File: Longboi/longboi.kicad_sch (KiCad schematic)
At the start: 190 parts, among them J2 ICSP_Header, K0 KEYSW, K1 KEYSW, K10 KEYSW, K11 KEYSW, K12 KEYSW, K13 KEYSW, K14 KEYSW, K15 KEYSW, K16 KEYSW, K17 KEYSW, K18 KEYSW, K19 KEYSW, K2 KEYSW, K20 KEYSW, K21 KEYSW, K22 KEYSW, K22-spacer1 KEYSW, K22-stepped1 KEYSW, K23 KEYSW, K24 KEYSW, K25 KEYSW, K26 KEYSW, K27 KEYSW, K28 KEYSW, K29 KEYSW, K3 KEYSW, K3-2uVert1 KEYSW, K30 KEYSW, K31 KEYSW, K32 KEYSW, K33 KEYSW, K34 KEYSW, K35 KEYSW, K36 KEYSW, K37 KEYSW, K38 KEYSW, K38-2uVert1 KEYSW, K39 KEYSW, K39-spacer1 KEYSW, K4 KEYSW, K4-spacer1 KEYSW, K40 KEYSW, K41 KEYSW, K42 KEYSW, K43 KEYSW, K44 KEYSW, K45 KEYSW, K46 KEYSW, K47 KEYSW, K48 KEYSW, K49 KEYSW, K5 KEYSW, K50 KEYSW, K51 KEYSW, K52 KEYSW, K52-1u1 KEYSW, K52-2u1 KEYSW, K53 KEYSW, K54 KEYSW, K55 KEYSW, K55-1.25 KEYSW, K55-spacer1 KEYSW, K56 KEYSW, K56-1.25 KEYSW, K57 KEYSW, K57-1.25 KEYSW, K57-1.5u1 KEYSW, K57-1u1 KEYSW, K58 KEYSW, K58-6u1 KEYSW, K58for1.25Row1 KEYSW, K59 KEYSW, K59-1.25u1 KEYSW, K59-7u1 KEYSW, K59Alt1 KEYSW, K6 KEYSW, K60 KEYSW, K60Alt1 KEYSW, K61 KEYSW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

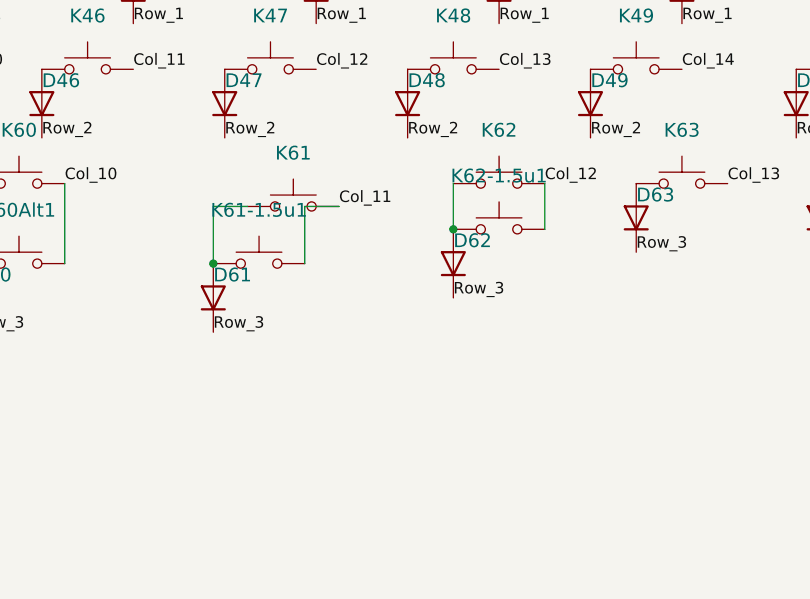
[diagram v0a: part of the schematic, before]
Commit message: update longboi to be slightly newer than ordered
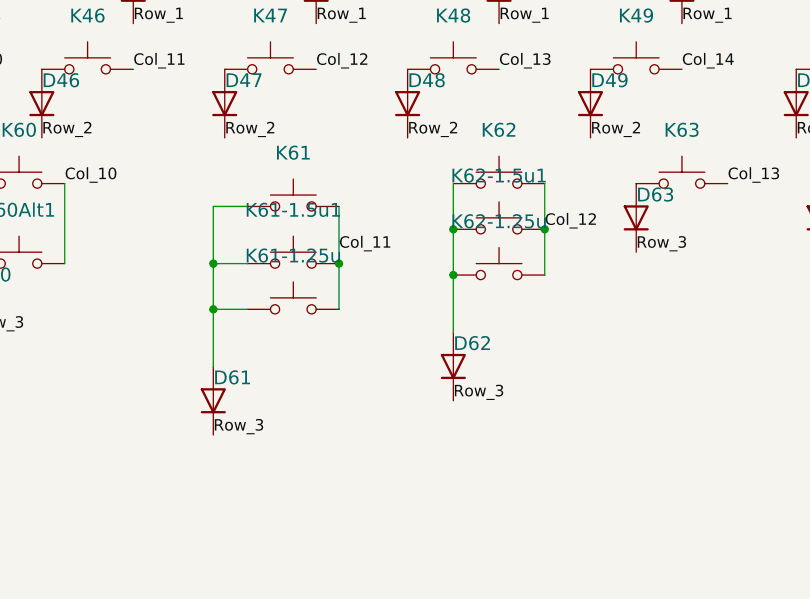
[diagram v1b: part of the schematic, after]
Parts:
- added K61-1.25u, K62-1.25u: KEYSW, MX_Only:MXOnly-1.25U-NoLED, symbol Switch:SW_Push
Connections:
- net Col_11: now also K61-1.25u.2
- net Col_12: now also K62-1.25u.2
- net at D62.2 (A), K62-1.5u1.1, K62.1: now also K62-1.25u.1
- net at D61.2 (A), K61-1.5u1.1, K61.1: now also K61-1.25u.1
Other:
- moved on the sheet: D61, D62, K61-1.5u1
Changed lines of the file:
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@@
   (junction (at 30.48 87.63) (diameter 0) (color 0 0 0 0)
   )
+  (junction (at 292.1 91.44) (diameter 0) (color 0 0 0 0)
+  )
   (junction (at 105.41 261.62) (diameter 0) (color 0 0 0 0)
   )
@@
   (junction (at 148.59 252.73) (diameter 0) (color 0 0 0 0)
   )
+  (junction (at 278.13 96.52) (diameter 0) (color 0 0 0 0)
+  )
   (junction (at 101.6 113.03) (diameter 0) (color 0 0 0 0)
   )
@@
   (junction (at 278.13 91.44) (diameter 0) (color 0 0 0 0)
   )
+  (junction (at 304.8 92.71) (diameter 0) (color 0 0 0 0)
+  )
   (junction (at 149.86 88.9) (diameter 0) (color 0 0 0 0)
   )
@@
   (junction (at 218.44 105.41) (diameter 0) (color 0 0 0 0)
   )
+  (junction (at 314.96 87.63) (diameter 0) (color 0 0 0 0)
+  )
   (junction (at 228.6 91.44) (diameter 0) (color 0 0 0 0)
   )
@@
     (stroke (width 0) (type default) (color 0 0 0 0))
   )
+  (wire (pts (xy 278.13 102.87) (xy 278.13 96.52))
+    (stroke (width 0) (type default) (color 0 0 0 0))
+  )
   (wire (pts (xy 228.6 91.44) (xy 228.6 82.55))
     (stroke (width 0) (type default) (color 0 0 0 0))
@@
     (stroke (width 0) (type default) (color 0 0 0 0))
   )
+  (wire (pts (xy 304.8 92.71) (xy 304.8 87.63))
+    (stroke (width 0) (type default) (color 0 0 0 0))
+  )
   (wire (pts (xy 403.86 35.56) (xy 405.13 35.56))
     (stroke (width 0) (type default) (color 0 0 0 0))
@@
     (stroke (width 0) (type default) (color 0 0 0 0))
   )
-  (wire (pts (xy 288.29 91.44) (xy 288.29 85.09))
-    (stroke (width 0) (type default) (color 0 0 0 0))
-  )
   (wire (pts (xy 152.4 229.87) (xy 152.4 218.44))
     (stroke (width 0) (type default) (color 0 0 0 0))
@@
     (stroke (width 0) (type default) (color 0 0 0 0))
   )
-  (wire (pts (xy 314.96 87.63) (xy 314.96 82.55))
+  (wire (pts (xy 314.96 92.71) (xy 314.96 87.63))
     (stroke (width 0) (type default) (color 0 0 0 0))
   )
@@
     (stroke (width 0) (type default) (color 0 0 0 0))
   )
+  (wire (pts (xy 304.8 99.06) (xy 304.8 92.71))
+    (stroke (width 0) (type default) (color 0 0 0 0))
+  )
   (wire (pts (xy 228.6 91.44) (xy 228.6 97.79))
     (stroke (width 0) (type default) (color 0 0 0 0))
@@
     (stroke (width 0) (type default) (color 0 0 0 0))
   )
+  (wire (pts (xy 292.1 85.09) (xy 292.1 91.44))
+    (stroke (width 0) (type default) (color 0 0 0 0))
+  )
   (wire (pts (xy 128.27 237.49) (xy 128.27 247.65))
     (stroke (width 0) (type default) (color 0 0 0 0))
@@
     (stroke (width 0) (type default) (color 0 0 0 0))
   )
+  (wire (pts (xy 292.1 96.52) (xy 292.1 91.44))
+    (stroke (width 0) (type default) (color 0 0 0 0))
+  )
   (wire (pts (xy 124.46 110.49) (xy 124.46 102.87))
     (stroke (width 0) (type default) (color 0 0 0 0))
@@
     (stroke (width 0) (type default) (color 0 0 0 0))
   )
+  (wire (pts (xy 281.94 96.52) (xy 278.13 96.52))
+    (stroke (width 0) (type default) (color 0 0 0 0))
+  )
   (wire (pts (xy 156.21 252.73) (xy 153.67 252.73))
     (stroke (width 0) (type default) (color 0 0 0 0))
   )
+  (wire (pts (xy 281.94 91.44) (xy 278.13 91.44))
+    (stroke (width 0) (type default) (color 0 0 0 0))
+  )
   (wire (pts (xy 134.62 218.44) (xy 134.62 242.57))
     (stroke (width 0) (type default) (color 0 0 0 0))
@@
     (stroke (width 0) (type default) (color 0 0 0 0))
   )
-  (wire (pts (xy 288.29 85.09) (xy 292.1 85.09))
-    (stroke (width 0) (type default) (color 0 0 0 0))
-  )
   (wire (pts (xy 91.44 48.26) (xy 91.44 44.45))
     (stroke (width 0) (type default) (color 0 0 0 0))
@@
     (stroke (width 0) (type default) (color 0 0 0 0))
   )
+  (wire (pts (xy 278.13 96.52) (xy 278.13 91.44))
+    (stroke (width 0) (type default) (color 0 0 0 0))
+  )
+  (wire (pts (xy 314.96 87.63) (xy 314.96 82.55))
+    (stroke (width 0) (type default) (color 0 0 0 0))
+  )
   (wire (pts (xy 123.19 247.65) (xy 123.19 257.81))
     (stroke (width 0) (type default) (color 0 0 0 0))
@@
     (effects (font (size 1.27 1.27)) (justify left bottom))
   )
-  (label "Row_3" (at 304.8 95.25 0)
+  (label "Row_3" (at 304.8 106.68 0)
     (effects (font (size 1.27 1.27)) (justify left bottom))
   )
@@
     (effects (font (size 1.27 1.27)) (justify left bottom))
   )
-  (label "Col_12" (at 314.96 82.55 0)
+  (label "Col_12" (at 314.96 87.63 0)
     (effects (font (size 1.27 1.27)) (justify left bottom))
   )
@@
     (effects (font (size 1.27 1.27)) (justify left bottom))
   )
-  (label "Col_11" (at 292.1 85.09 0)
+  (label "Col_11" (at 292.1 90.17 0)
     (effects (font (size 1.27 1.27)) (justify left bottom))
   )
@@
     (effects (font (size 1.27 1.27)) (justify left bottom))
   )
-  (label "Row_3" (at 278.13 99.06 0)
+  (label "Row_3" (at 278.13 110.49 0)
     (effects (font (size 1.27 1.27)) (justify left bottom))
   )
@@
     (pin "2")
   )
-  (symbol (lib_id "Device:D") (at 304.8 91.44 90) (unit 1)
+  (symbol (lib_id "Device:D") (at 304.8 102.87 90) (unit 1)
     (in_bom yes) (on_board yes)
-    (property "Reference" "D62" (id 0) (at 304.8 88.9 90)
+    (property "Reference" "D62" (id 0) (at 304.8 100.33 90)
       (effects (font (size 1.524 1.524)) (justify right))
     )
-    (property "Value" "SOD-323F" (id 1) (at 306.07 97.79 90)
+    (property "Value" "SOD-323F" (id 1) (at 306.07 109.22 90)
       (effects (font (size 1.524 1.524)) (justify right) hide)
     )
-    (property "Footprint" "Diode_SMD:D_SOD-323F" (id 2) (at 304.8 101.6 0)
+    (property "Footprint" "Diode_SMD:D_SOD-323F" (id 2) (at 304.8 113.03 0)
       (effects (font (size 1.524 1.524)) hide)
     )
-    (property "Datasheet" "" (id 3) (at 304.8 101.6 0)
+    (property "Datasheet" "" (id 3) (at 304.8 113.03 0)
       (effects (font (size 1.524 1.524)))
     )
@@
     (pin "2")
   )
-  (symbol (lib_id "Device:D") (at 278.13 95.25 90) (unit 1)
+  (symbol (lib_id "Device:D") (at 278.13 106.68 90) (unit 1)
     (in_bom yes) (on_board yes)
-    (property "Reference" "D61" (id 0) (at 278.13 92.71 90)
+    (property "Reference" "D61" (id 0) (at 278.13 104.14 90)
       (effects (font (size 1.524 1.524)) (justify right))
     )
-    (property "Value" "SOD-323F" (id 1) (at 279.4 101.6 90)
+    (property "Value" "SOD-323F" (id 1) (at 279.4 113.03 90)
       (effects (font (size 1.524 1.524)) (justify right) hide)
     )
-    (property "Footprint" "Diode_SMD:D_SOD-323F" (id 2) (at 278.13 105.41 0)
+    (property "Footprint" "Diode_SMD:D_SOD-323F" (id 2) (at 278.13 116.84 0)
       (effects (font (size 1.524 1.524)) hide)
     )
-    (property "Datasheet" "" (id 3) (at 278.13 105.41 0)
+    (property "Datasheet" "" (id 3) (at 278.13 116.84 0)
       (effects (font (size 1.524 1.524)))
     )
@@
     (pin "2")
   )
-  (symbol (lib_id "Switch:SW_Push") (at 283.21 91.44 0) (unit 1)
+  (symbol (lib_id "Switch:SW_Push") (at 287.02 91.44 0) (unit 1)
     (in_bom yes) (on_board yes)
-    (property "Reference" "K61-1.5u1" (id 0) (at 283.21 85.5218 0)
+    (property "Reference" "K61-1.5u1" (id 0) (at 287.02 85.5218 0)
       (effects (font (size 1.524 1.524)))
     )
-    (property "Value" "KEYSW" (id 1) (at 283.21 93.98 0)
+    (property "Value" "KEYSW" (id 1) (at 287.02 93.98 0)
       (effects (font (size 1.524 1.524)) hide)
     )
-    (property "Footprint" "MX_Only:MXOnly-1.5U-NoLED" (id 2) (at 283.21 91.44 0)
+    (property "Footprint" "MX_Only:MXOnly-1.5U-NoLED" (id 2) (at 287.02 91.44 0)
       (effects (font (size 1.524 1.524)) hide)
     )
-    (property "Datasheet" "" (id 3) (at 283.21 91.44 0)
+    (property "Datasheet" "" (id 3) (at 287.02 91.44 0)
       (effects (font (size 1.524 1.524)))
     )
@@
     (pin "2")
   )
+  (symbol (lib_id "Switch:SW_Push") (at 309.88 92.71 0) (unit 1)
+    (in_bom yes) (on_board yes)
+    (property "Reference" "K62-1.25u" (id 0) (at 309.88 86.7918 0)
+      (effects (font (size 1.524 1.524)))
+    )
+    (property "Value" "KEYSW" (id 1) (at 309.88 95.25 0)
+      (effects (font (size 1.524 1.524)) hide)
+    )
+    (property "Footprint" "MX_Only:MXOnly-1.25U-NoLED" (id 2) (at 309.88 92.71 0)
+      (effects (font (size 1.524 1.524)) hide)
+    )
+    (property "Datasheet" "" (id 3) (at 309.88 92.71 0)
+      (effects (font (size 1.524 1.524)))
+    )
+    (pin "1")
+    (pin "2")
+  )
+  (symbol (lib_id "Switch:SW_Push") (at 287.02 96.52 0) (unit 1)
+    (in_bom yes) (on_board yes)
+    (property "Reference" "K61-1.25u" (id 0) (at 287.02 90.6018 0)
+      (effects (font (size 1.524 1.524)))
+    )
+    (property "Value" "KEYSW" (id 1) (at 287.02 99.06 0)
+      (effects (font (size 1.524 1.524)) hide)
+    )
+    (property "Footprint" "MX_Only:MXOnly-1.25U-NoLED" (id 2) (at 287.02 96.52 0)
+      (effects (font (size 1.524 1.524)) hide)
+    )
+    (property "Datasheet" "" (id 3) (at 287.02 96.52 0)
+      (effects (font (size 1.524 1.524)))
+    )
+    (pin "1")
+    (pin "2")
+  )
   (symbol (lib_id "Switch:SW_Push") (at 35.56 87.63 0) (unit 1)
     (in_bom yes) (on_board yes)
@@
       (reference "K61-1.5u1") (unit 1) (value "KEYSW") (footprint "MX_Only:MXOnly-1.5U-NoLED")
     )
+    (path "/94c26993-bb91-483b-ab9b-cc98b43c45dd"
+      (reference "K61-1.25u") (unit 1) (value "KEYSW") (footprint "MX_Only:MXOnly-1.25U-NoLED")
+    )
     (path "/00000000-0000-0000-0000-000062166a78"
       (reference "K62") (unit 1) (value "KEYSW") (footprint "MX_Only:MXOnly-1U-NoLED")
@@
       (reference "K62-1.5u1") (unit 1) (value "KEYSW") (footprint "MX_Only:MXOnly-1.5U-NoLED")
     )
+    (path "/710abe27-ce29-434f-9460-1c18893d781d"
+      (reference "K62-1.25u") (unit 1) (value "KEYSW") (footprint "MX_Only:MXOnly-1.25U-NoLED")
+    )
     (path "/00000000-0000-0000-0000-000062166a74"
